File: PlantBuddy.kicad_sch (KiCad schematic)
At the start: 70 parts, among them J1 USB_C_Receptacle_USB2.0, J101 JST, J102 J-Link SWD, J4 External, Q101 DMG1012T, SW1 SW_Push, U1 LTR-303ALS-01, U101 RT9080-33GJ5, U102 nRF52832-QFxx, U104 XB5350A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

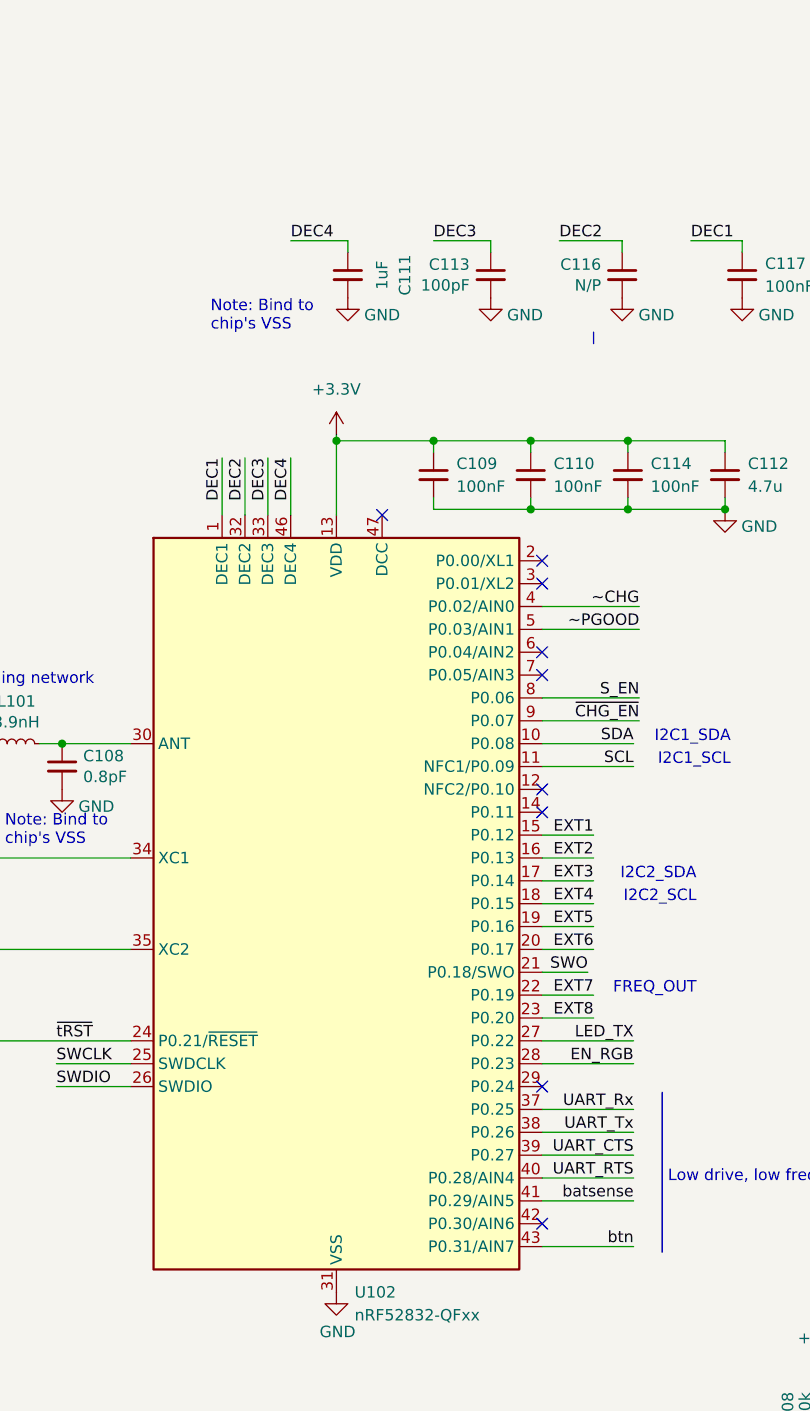
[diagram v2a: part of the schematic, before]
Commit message: Major PCB changes.
- Added inductor for nRF52 DCDC converter.
- Moved USB-C connector to bottom left.
- Moved USB charger and battery protection IC.
- Moved USB-to-serial converter.
- Changed pinout to simplify routing.
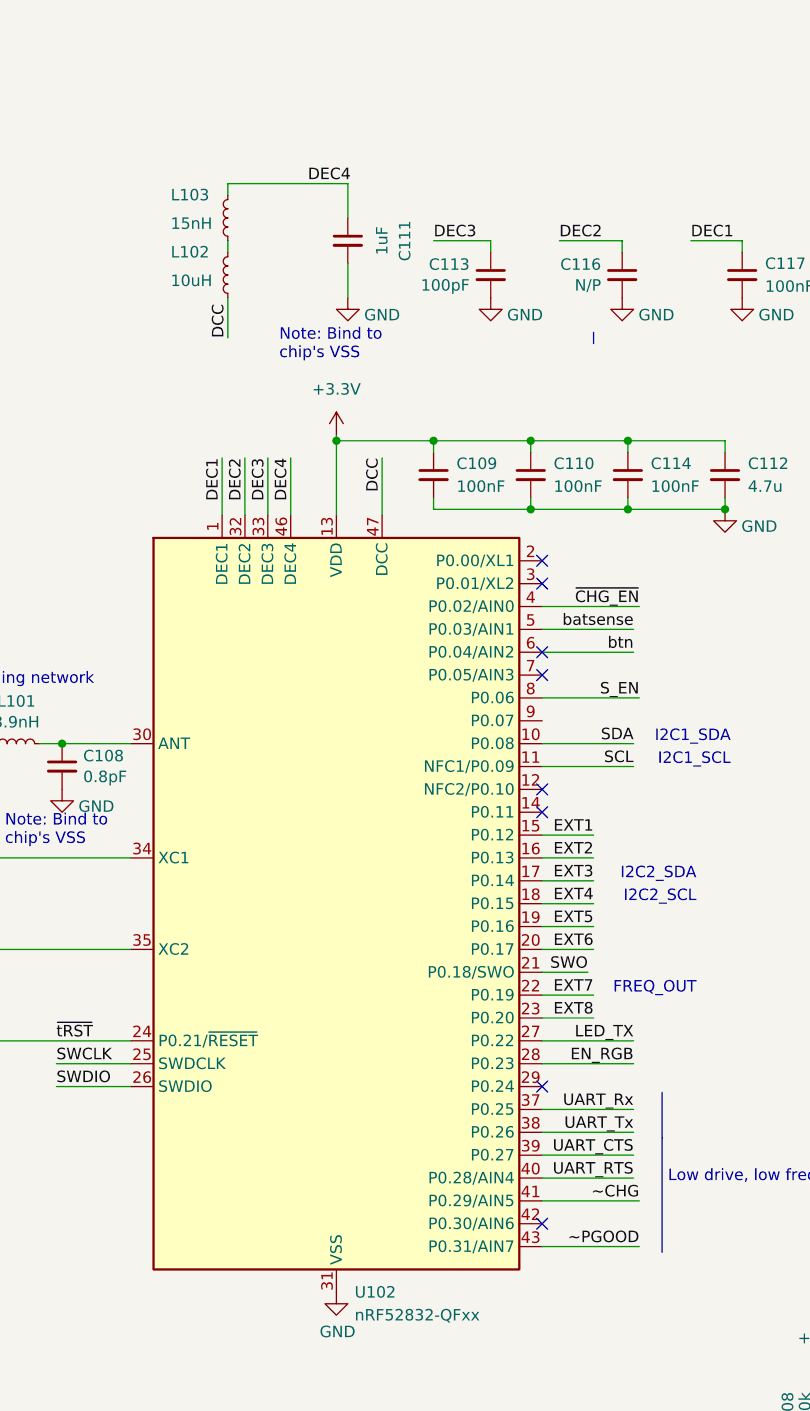
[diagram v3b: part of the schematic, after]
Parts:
- added L102: 10uH, Inductor_SMD:L_0603_1608Metric, symbol Device:L_Small
- added L103: 15nH, Inductor_SMD:L_0402_1005Metric, symbol Device:L_Small
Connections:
- net DEC4: now also L103.1
- net batsense: now also U102.5 (P0.03/AIN1); no longer U102.41 (P0.29/AIN5)
- net btn: now also U102.6 (P0.04/AIN2); no longer U102.43 (P0.31/AIN7)
- net ~CHG: now also U102.41 (P0.29/AIN5); no longer U102.4 (P0.02/AIN0)
- net ~PGOOD: now also U102.43 (P0.31/AIN7); no longer U102.5 (P0.03/AIN1)
- net ~{CHG_EN}: now also U102.4 (P0.02/AIN0); no longer U102.9 (P0.07)
- net DCC: now reaches U102.47 (DCC)
- net DCC: now also L102.2
- new net: L102.1, L103.2
- no-connect marks 29 -> 28
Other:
- moved on the sheet: C111
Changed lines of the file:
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@@
   (no_connect (at 162.56 64.135))
   (no_connect (at 162.56 66.675))
-  (no_connect (at 109.855 155.575))
   (no_connect (at 282.575 273.05))
   (no_connect (at 387.223 116.586))
@@
     (stroke (width 0) (type default) (color 0 0 0 0))
   )
+  (wire (pts (xy 92.71 118.745) (xy 106.045 118.745))
+    (stroke (width 0) (type default) (color 0 0 0 0))
+  )
   (wire (pts (xy 390.398 60.325) (xy 398.018 60.325))
     (stroke (width 0) (type default) (color 0 0 0 0))
@@
     (stroke (width 0) (type default) (color 0 0 0 0))
   )
-  (wire (pts (xy 127.635 231.775) (xy 137.795 231.775))
+  (wire (pts (xy 127.635 168.275) (xy 137.795 168.275))
     (stroke (width 0) (type default) (color 0 0 0 0))
   )
@@
     (stroke (width 0) (type default) (color 0 0 0 0))
   )
-  (wire (pts (xy 127.635 236.855) (xy 137.795 236.855))
+  (wire (pts (xy 127.635 170.815) (xy 137.795 170.815))
     (stroke (width 0) (type default) (color 0 0 0 0))
   )
@@
     (stroke (width 0) (type default) (color 0 0 0 0))
   )
-  (wire (pts (xy 127.635 178.435) (xy 138.43 178.435))
+  (wire (pts (xy 127.635 165.735) (xy 138.43 165.735))
     (stroke (width 0) (type default) (color 0 0 0 0))
   )
@@
     (stroke (width 0) (type default) (color 0 0 0 0))
   )
+  (wire (pts (xy 92.71 126.365) (xy 92.71 125.095))
+    (stroke (width 0) (type default) (color 0 0 0 0))
+  )
   (wire (pts (xy 372.618 24.765) (xy 375.158 24.765))
     (stroke (width 0) (type default) (color 0 0 0 0))
@@
     (stroke (width 0) (type default) (color 0 0 0 0))
   )
+  (wire (pts (xy 106.045 127.635) (xy 106.045 131.445))
+    (stroke (width 0) (type default) (color 0 0 0 0))
+  )
   (wire (pts (xy 329.057 128.524) (xy 334.137 128.524))
     (stroke (width 0) (type default) (color 0 0 0 0))
@@
     (stroke (width 0) (type default) (color 0 0 0 0))
   )
-  (wire (pts (xy 127.635 165.735) (xy 138.43 165.735))
+  (wire (pts (xy 127.635 231.775) (xy 138.43 231.775))
     (stroke (width 0) (type default) (color 0 0 0 0))
   )
@@
     (stroke (width 0) (type default) (color 0 0 0 0))
   )
+  (wire (pts (xy 92.71 120.015) (xy 92.71 118.745))
+    (stroke (width 0) (type default) (color 0 0 0 0))
+  )
   (wire (pts (xy 320.675 99.695) (xy 320.675 100.965))
     (stroke (width 0) (type default) (color 0 0 0 0))
@@
     (stroke (width 0) (type default) (color 0 0 0 0))
   )
-  (wire (pts (xy 106.045 125.095) (xy 106.045 126.365))
+  (wire (pts (xy 106.045 118.745) (xy 106.045 122.555))
     (stroke (width 0) (type default) (color 0 0 0 0))
   )
@@
     (stroke (width 0) (type default) (color 0 0 0 0))
   )
+  (wire (pts (xy 109.855 149.225) (xy 109.855 155.575))
+    (stroke (width 0) (type default) (color 0 0 0 0))
+  )
   (wire (pts (xy 39.37 207.645) (xy 42.545 207.645))
     (stroke (width 0) (type default) (color 0 0 0 0))
@@
     (stroke (width 0) (type default) (color 0 0 0 0))
   )
-  (wire (pts (xy 127.635 168.275) (xy 138.43 168.275))
+  (wire (pts (xy 127.635 236.855) (xy 138.43 236.855))
     (stroke (width 0) (type default) (color 0 0 0 0))
   )
@@
     (stroke (width 0) (type default) (color 0 0 0 0))
   )
-  (wire (pts (xy 99.695 125.095) (xy 106.045 125.095))
-    (stroke (width 0) (type default) (color 0 0 0 0))
-  )
   (wire (pts (xy 314.325 99.695) (xy 320.675 99.695))
     (stroke (width 0) (type default) (color 0 0 0 0))
@@
     (stroke (width 0) (type default) (color 0 0 0 0))
   )
+  (wire (pts (xy 92.71 131.445) (xy 92.71 135.89))
+    (stroke (width 0) (type default) (color 0 0 0 0))
+  )
   (wire (pts (xy 266.827 99.949) (xy 273.177 99.949))
     (stroke (width 0) (type default) (color 0 0 0 0))
@@
     (effects (font (size 1.27 1.27)) (justify right bottom))
   )
-  (text "Note: Bind to\nchip's VSS" (at 90.805 135.255 0)
+  (text "Note: Bind to\nchip's VSS" (at 98.425 138.43 0)
     (effects (font (size 1.27 1.27)) (justify left bottom))
   )
@@
     (effects (font (size 1.27 1.27) (thickness 0.254) bold) (justify right bottom))
   )
-  (label "btn" (at 137.795 236.855 180)
+  (label "btn" (at 137.795 170.815 180)
     (effects (font (size 1.27 1.27)) (justify right bottom))
   )
@@
     (effects (font (size 1.27 1.27)) (justify right bottom))
   )
+  (label "DCC" (at 109.855 149.225 270)
+    (effects (font (size 1.27 1.27)) (justify right bottom))
+  )
   (label "EXT7" (at 329.057 141.224 0)
     (effects (font (size 1.27 1.27)) (justify left bottom))
   )
+  (label "DCC" (at 92.71 135.89 90)
+    (effects (font (size 1.27 1.27)) (justify left bottom))
+  )
   (label "UART_CTS" (at 137.795 226.695 180)
     (effects (font (size 1.27 1.27)) (justify right bottom))
@@
     (effects (font (size 1.27 1.27)) (justify left bottom))
   )
-  (label "batsense" (at 137.795 231.775 180)
+  (label "batsense" (at 137.795 168.275 180)
     (effects (font (size 1.27 1.27)) (justify right bottom))
   )
@@
     (effects (font (size 1.27 1.27)) (justify right bottom))
   )
-  (label "~PGOOD" (at 138.43 168.275 180)
+  (label "~PGOOD" (at 138.43 236.855 180)
     (effects (font (size 1.27 1.27)) (justify right bottom))
   )
@@
     (effects (font (size 1.27 1.27)) (justify right bottom))
   )
-  (label "~CHG" (at 138.43 165.735 180)
+  (label "~CHG" (at 138.43 231.775 180)
     (effects (font (size 1.27 1.27)) (justify right bottom))
   )
@@
     (effects (font (size 1.27 1.27)) (justify right bottom))
   )
-  (label "DEC4" (at 99.695 125.095 0)
+  (label "DEC4" (at 101.6 118.745 0)
     (effects (font (size 1.27 1.27)) (justify left bottom))
   )
@@
     (effects (font (size 1.27 1.27)) (justify right bottom))
   )
-  (label "~{CHG_EN}" (at 138.43 178.435 180)
+  (label "~{CHG_EN}" (at 138.43 165.735 180)
     (effects (font (size 1.27 1.27)) (justify right bottom))
   )
@@
     (pin "1")
   )
+  (symbol (lib_id "Device:L_Small") (at 92.71 128.905 0) (mirror y) (unit 1)
+    (in_bom yes) (on_board yes)
+    (property "Reference" "L102" (id 0) (at 86.36 126.365 0)
+      (effects (font (size 1.27 1.27)) (justify right))
+    )
+    (property "Value" "10uH" (id 1) (at 86.36 129.54 0)
+      (effects (font (size 1.27 1.27)) (justify right))
+    )
+    (property "Footprint" "Inductor_SMD:L_0603_1608Metric" (id 2) (at 92.71 128.905 0)
+      (effects (font (size 1.27 1.27)) hide)
+    )
+    (property "Datasheet" "~" (id 3) (at 92.71 128.905 0)
+      (effects (font (size 1.27 1.27)) hide)
+    )
+    (property "LCSC" "C223240" (id 4) (at 92.71 128.905 0)
+      (effects (font (size 1.27 1.27)) hide)
+    )
+    (pin "1")
+    (pin "2")
+  )
   (symbol (lib_id "LMS33460:LMS33460MG") (at 36.195 228.6 0) (unit 1)
     (in_bom yes) (on_board yes) (fields_autoplaced)
@@
     (pin "2")
   )
+  (symbol (lib_id "Device:L_Small") (at 92.71 122.555 0) (mirror y) (unit 1)
+    (in_bom yes) (on_board yes)
+    (property "Reference" "L103" (id 0) (at 86.36 120.015 0)
+      (effects (font (size 1.27 1.27)) (justify right))
+    )
+    (property "Value" "15nH" (id 1) (at 86.36 123.19 0)
+      (effects (font (size 1.27 1.27)) (justify right))
+    )
+    (property "Footprint" "Inductor_SMD:L_0402_1005Metric" (id 2) (at 92.71 122.555 0)
+      (effects (font (size 1.27 1.27)) hide)
+    )
+    (property "Datasheet" "~" (id 3) (at 92.71 122.555 0)
+      (effects (font (size 1.27 1.27)) hide)
+    )
+    (property "LCSC" "C27143" (id 4) (at 92.71 122.555 0)
+      (effects (font (size 1.27 1.27)) hide)
+    )
+    (pin "1")
+    (pin "2")
+  )
   (symbol (lib_id "Transistor_FET:DMG1012T") (at 377.063 129.286 0) (unit 1)
     (in_bom yes) (on_board yes) (fields_autoplaced)
@@
     (pin "2")
   )
-  (symbol (lib_id "Device:C_Small") (at 106.045 128.905 0) (unit 1)
+  (symbol (lib_id "Device:C_Small") (at 106.045 125.095 0) (unit 1)
     (in_bom yes) (on_board yes) (fields_autoplaced)
-    (property "Reference" "C111" (id 0) (at 112.395 128.9113 90))
-    (property "Value" "1uF" (id 1) (at 109.855 128.9113 90))
-    (property "Footprint" "Capacitor_SMD:C_0402_1005Metric" (id 2) (at 106.045 128.905 0)
+    (property "Reference" "C111" (id 0) (at 112.395 125.1013 90))
+    (property "Value" "1uF" (id 1) (at 109.855 125.1013 90))
+    (property "Footprint" "Capacitor_SMD:C_0402_1005Metric" (id 2) (at 106.045 125.095 0)
       (effects (font (size 1.27 1.27)) hide)
     )
-    (property "Datasheet" "~" (id 3) (at 106.045 128.905 0)
+    (property "Datasheet" "~" (id 3) (at 106.045 125.095 0)
       (effects (font (size 1.27 1.27)) hide)
     )
-    (property "LCSC" "C52923" (id 4) (at 106.045 128.905 0)
+    (property "LCSC" "C52923" (id 4) (at 106.045 125.095 0)
       (effects (font (size 1.27 1.27)) hide)
     )
-    (property "MPN" "CC0603KRX7R9BB104" (id 5) (at 106.045 128.905 0)
+    (property "MPN" "CC0603KRX7R9BB104" (id 5) (at 106.045 125.095 0)
       (effects (font (size 1.27 1.27)) hide)
     )
@@
       (reference "L101") (unit 1) (value "3.9nH") (footprint "Inductor_SMD:L_0402_1005Metric")
     )
+    (path "/127679e8-359f-42a4-870a-60c4bf70f089"
+      (reference "L102") (unit 1) (value "10uH") (footprint "Inductor_SMD:L_0603_1608Metric")
+    )
+    (path "/4425fbd4-9ddd-4e4a-b74b-b7928ff59221"
+      (reference "L103") (unit 1) (value "15nH") (footprint "Inductor_SMD:L_0402_1005Metric")
+    )
     (path "/44b22f98-6e17-4e70-b963-0e4442cb30c5"

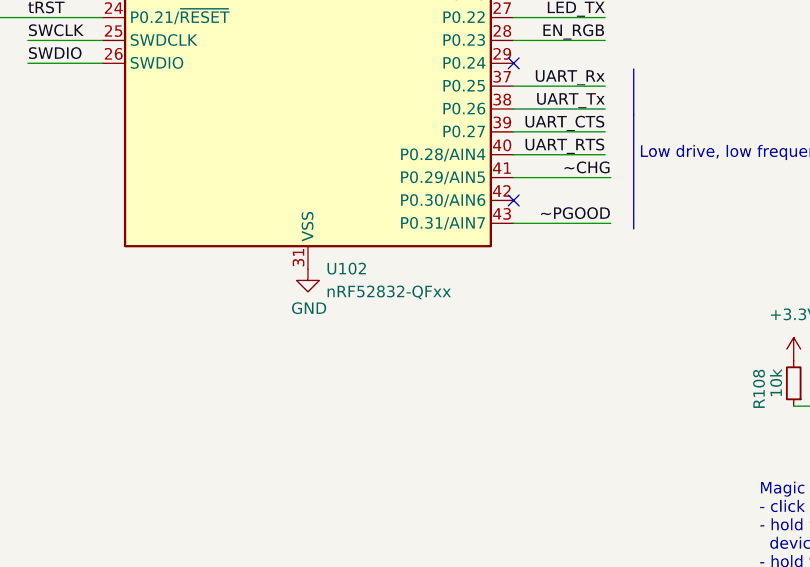
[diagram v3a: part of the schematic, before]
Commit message: Added proper MPN for Nordic chip
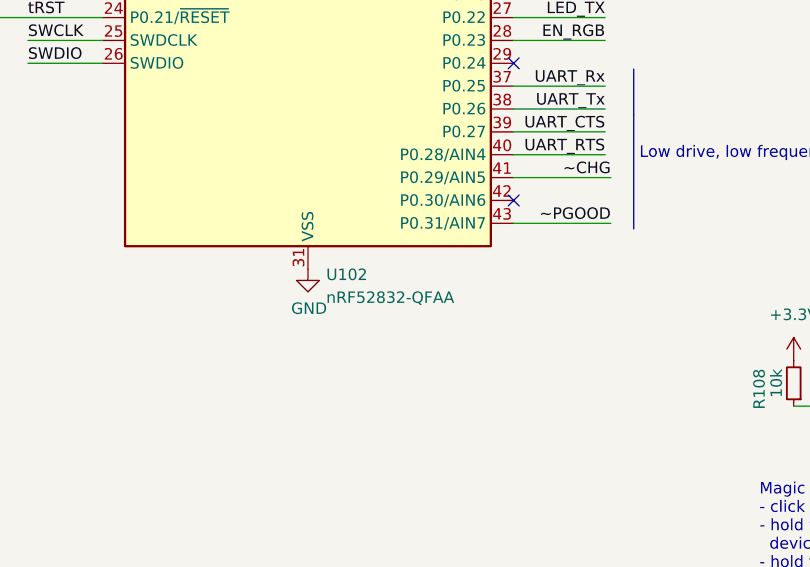
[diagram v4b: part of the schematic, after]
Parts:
- U102: value nRF52832-QFxx -> nRF52832-QFAA
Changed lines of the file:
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@@
   (symbol (lib_id "MCU_Nordic:nRF52832-QFxx") (at 104.775 198.755 0) (unit 1)
     (in_bom yes) (on_board yes) (fields_autoplaced)
-    (property "Reference" "U102" (id 0) (at 106.7944 241.935 0)
-      (effects (font (size 1.27 1.27)) (justify left))
-    )
-    (property "Value" "nRF52832-QFxx" (id 1) (at 106.7944 244.475 0)
+    (property "Reference" "U102" (id 0) (at 106.7944 242.57 0)
+      (effects (font (size 1.27 1.27)) (justify left))
+    )
+    (property "Value" "nRF52832-QFAA" (id 1) (at 106.7944 245.11 0)
       (effects (font (size 1.27 1.27)) (justify left))
     )
@@
     )
     (path "/77149749-28f7-48a0-89a9-bfe419d97e75"
-      (reference "U102") (unit 1) (value "nRF52832-QFxx") (footprint "Package_DFN_QFN:QFN-48-1EP_6x6mm_P0.4mm_EP4.6x4.6mm")
+      (reference "U102") (unit 1) (value "nRF52832-QFAA") (footprint "Package_DFN_QFN:QFN-48-1EP_6x6mm_P0.4mm_EP4.6x4.6mm")
     )
     (path "/dff537c4-3af9-41c9-9fd5-981d59d391bc"

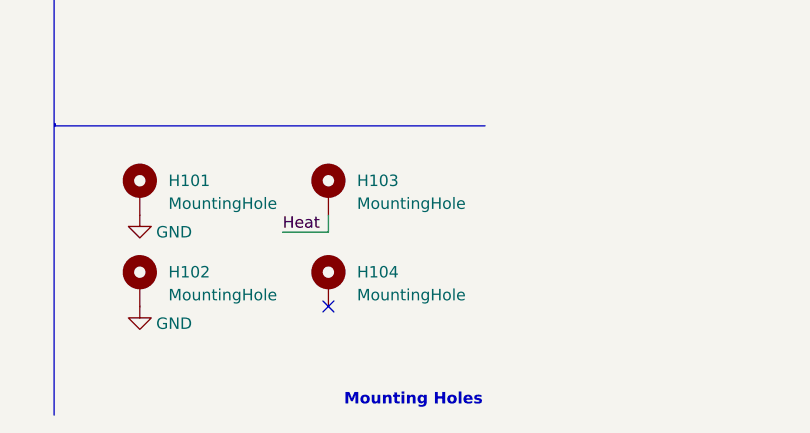
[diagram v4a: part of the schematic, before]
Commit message: Moved antenna
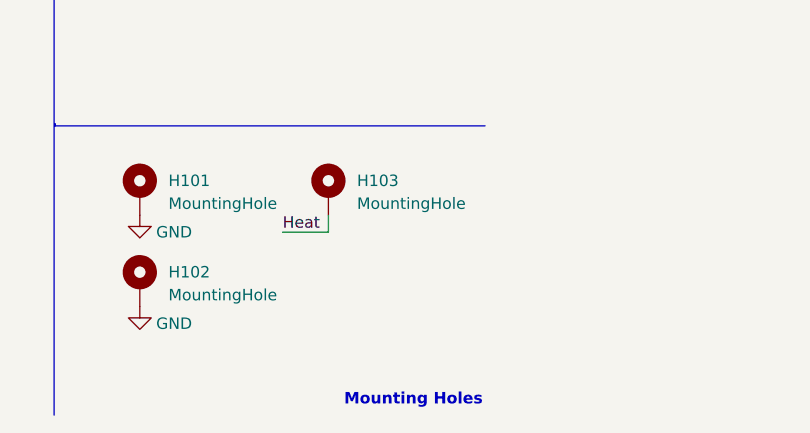
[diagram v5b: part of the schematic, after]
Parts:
- removed H104: MountingHole, MountingHole:MountingHole_2.2mm_M2_DIN965_Pad, symbol Mechanical:MountingHole_Pad
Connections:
- no-connect marks 28 -> 27
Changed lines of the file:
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@@
   (no_connect (at 162.56 64.135))
   (no_connect (at 162.56 66.675))
-  (no_connect (at 282.575 273.05))
   (no_connect (at 387.223 116.586))
   (no_connect (at 162.56 43.815))
@@
     (stroke (width 0) (type default) (color 0 0 0 0))
   )
-  (wire (pts (xy 302.133 42.545) (xy 304.673 42.545))
-    (stroke (width 0) (type default) (color 0 0 0 0))
-  )
   (wire (pts (xy 30.48 207.645) (xy 34.29 207.645))
     (stroke (width 0) (type default) (color 0 0 0 0))
@@
     (stroke (width 0) (type default) (color 0 0 0 0))
   )
+  (wire (pts (xy 302.133 42.545) (xy 304.673 42.545))
+    (stroke (width 0) (type default) (color 0 0 0 0))
+  )
   (wire (pts (xy 261.493 41.275) (xy 261.493 42.545))
     (stroke (width 0) (type default) (color 0 0 0 0))
@@
     (pin "2")
   )
-  (symbol (lib_id "Mechanical:MountingHole_Pad") (at 282.575 270.51 0) (unit 1)
-    (in_bom yes) (on_board yes) (fields_autoplaced)
-    (property "Reference" "H104" (id 0) (at 285.75 269.2399 0)
-      (effects (font (size 1.27 1.27)) (justify left))
-    )
-    (property "Value" "MountingHole" (id 1) (at 285.75 271.7799 0)
-      (effects (font (size 1.27 1.27)) (justify left))
-    )
-    (property "Footprint" "MountingHole:MountingHole_2.2mm_M2_DIN965_Pad" (id 2) (at 282.575 270.51 0)
-      (effects (font (size 1.27 1.27)) hide)
-    )
-    (property "Datasheet" "~" (id 3) (at 282.575 270.51 0)
-      (effects (font (size 1.27 1.27)) hide)
-    )
-    (pin "1")
-  )
   (symbol (lib_id "Connector:TestPoint_Small") (at 149.86 14.478 0) (mirror x) (unit 1)
     (in_bom yes) (on_board yes) (fields_autoplaced)
@@
       (reference "H103") (unit 1) (value "MountingHole") (footprint "MountingHole:MountingHole_2.2mm_M2_DIN965_Pad")
     )
-    (path "/6cfe9ef2-8926-4f8d-8ff8-2f362caa61a1"
-      (reference "H104") (unit 1) (value "MountingHole") (footprint "MountingHole:MountingHole_2.2mm_M2_DIN965_Pad")
-    )
     (path "/4138c96d-aa03-4df3-a048-35a223d1d760"
